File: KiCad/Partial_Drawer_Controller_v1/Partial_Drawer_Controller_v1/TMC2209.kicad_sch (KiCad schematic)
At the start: 14 parts, among them U11 TMC2209-LA

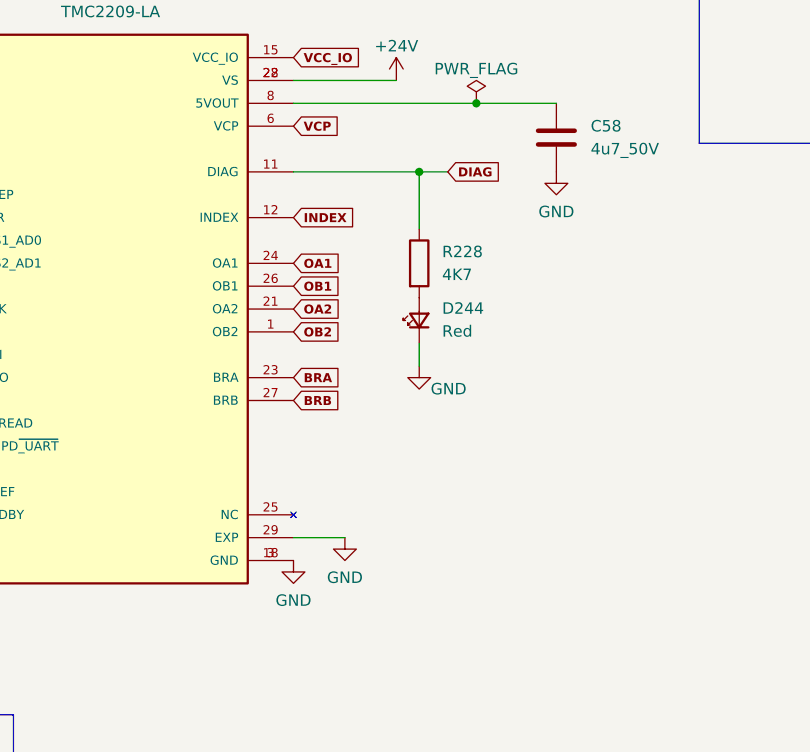
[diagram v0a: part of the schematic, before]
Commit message: feat: adds M2 mounting holes to partial_drawer_controller and minor adjustments
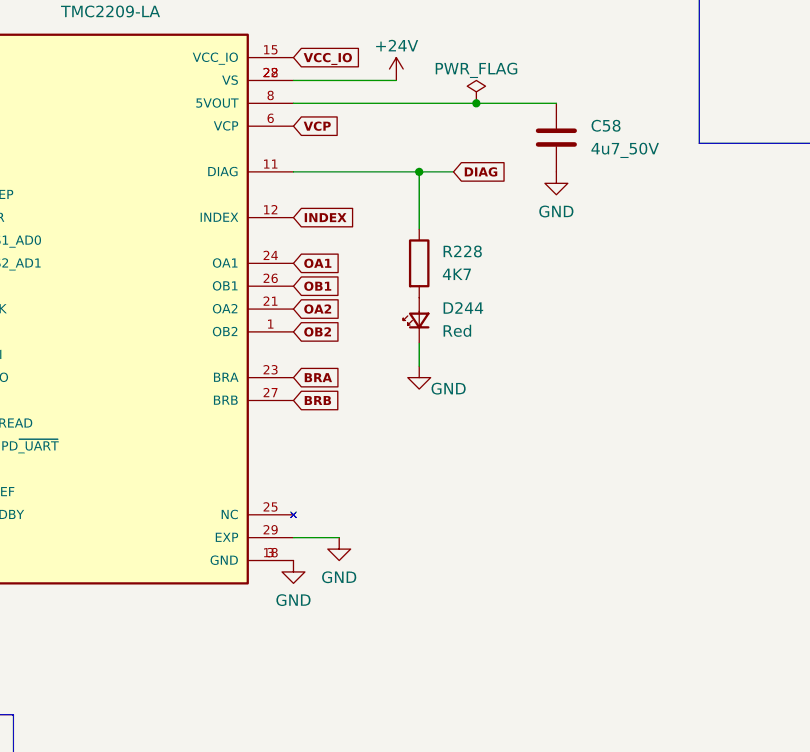
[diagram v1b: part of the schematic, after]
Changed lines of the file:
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@@
 	(wire
 		(pts
-			(xy 131.445 68.58) (xy 128.27 68.58)
+			(xy 132.08 68.58) (xy 128.27 68.58)
 		)
 		(stroke
@@
 	(wire
 		(pts
-			(xy 114.3 109.22) (xy 120.015 109.22)
+			(xy 114.3 109.22) (xy 119.38 109.22)
 		)
 		(stroke
@@
 	(global_label "DIAG"
 		(shape input)
-		(at 131.445 68.58 0)
+		(at 132.08 68.58 0)
 		(fields_autoplaced yes)
 		(effects
@@
 		)
 		(property "Intersheetrefs" "${INTERSHEET_REFS}"
-			(at 137.4036 68.58 0)
+			(at 138.0386 68.58 0)
 			(effects
 				(font
@@
 	(symbol
 		(lib_id "power:GND")
-		(at 120.015 109.22 0)
+		(at 119.38 109.22 0)
 		(unit 1)
 		(exclude_from_sim no)
@@
 		(fields_autoplaced yes)
 		(property "Reference" "#PWR0229"
-			(at 120.015 115.57 0)
+			(at 119.38 115.57 0)
 			(effects
 				(font
@@
 		)
 		(property "Value" "GND"
-			(at 120.015 113.665 0)
+			(at 119.38 113.665 0)
 			(effects
 				(font
@@
 		)
 		(property "Footprint" ""
-			(at 120.015 109.22 0)
+			(at 119.38 109.22 0)
 			(effects
 				(font
@@
 		)
 		(property "Datasheet" ""
-			(at 120.015 109.22 0)
+			(at 119.38 109.22 0)
 			(effects
 				(font
@@
 		)
 		(property "Description" ""
-			(at 120.015 109.22 0)
+			(at 119.38 109.22 0)
 			(effects
 				(font

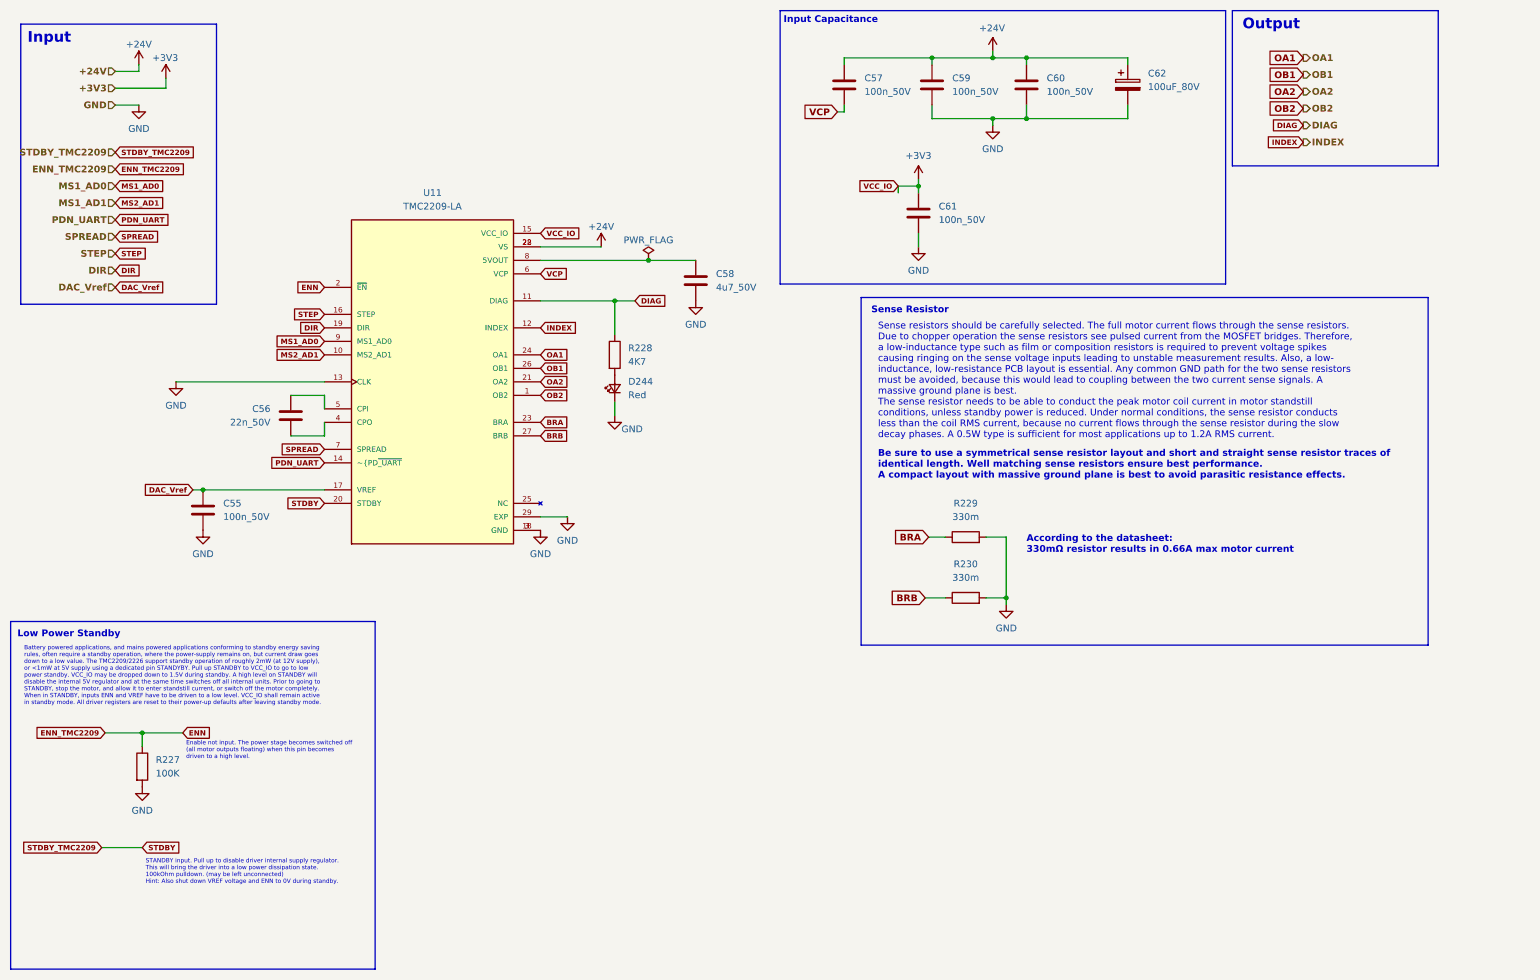
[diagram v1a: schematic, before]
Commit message: feat: minor adjustments and new export of manufacturing files for `Partial_Drawer_controller_v1`
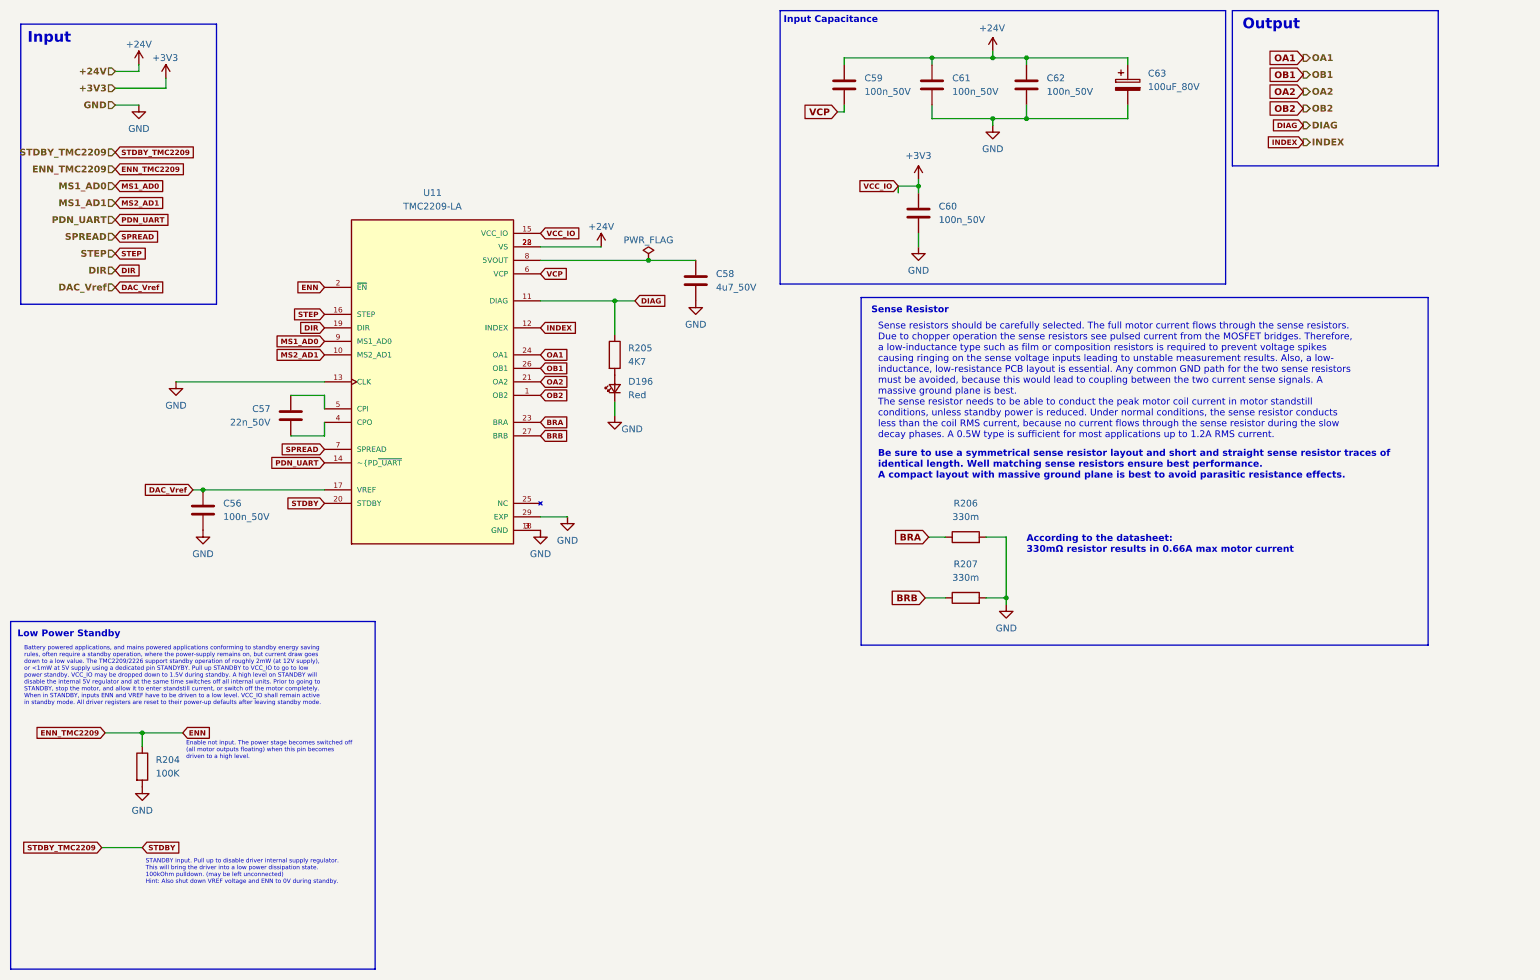
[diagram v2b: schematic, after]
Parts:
- renumbered C55 to C56, C56 to C57, C57 to C59, C61 to C60, C59 to C61, C60 to C62, C62 to C63, D244 to D196, R227 to R204, R228 to R205, R229 to R206, R230 to R207

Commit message: feat: replaces `CP_Elec_12.5x13.5` with `CP_Elec_10x10` for `Partial_Drawer_Controller_v1`
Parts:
- C63: footprint Robast:CP_Elec_12.5x13.5 -> Capacitor_SMD:CP_Elec_10x10; MPN VZH101M1KTR-1313 -> VZH101M1KTR-1010; OC_LCSC C249839 -> C249838; OC_MOUSER (none) -> 140-VZH101M1KTR1010
